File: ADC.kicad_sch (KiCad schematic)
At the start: 5 parts, among them J10 TBP03R2-350-03BE, J7 TBP03R2-350-03BE, J8 TBP03R2-350-03BE, J9 TBP03R2-350-03BE, U4 ADS1115IDGS

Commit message: Worked on PCB Layout
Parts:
- J10, J7, J8, J9: footprint TBP03R2-350-03BE:CUI_TBP03R2-350-03BE -> TBP03R2_350_03BE(1):CUI_TBP03R2-350-03BE
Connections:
- removed net Signal: J10.2, J7.2, J8.2, J9.2, U4.4 (AIN0), U4.5 (AIN1), U4.6 (AIN2), U4.7 (AIN3)
- new net Signal 1: J7.2, U4.4 (AIN0)
- new net Signal 2: J8.2, U4.5 (AIN1)
- new net Signal 3: J9.2, U4.6 (AIN2)
- new net Signal 4: J10.2, U4.7 (AIN3)
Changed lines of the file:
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@@
+	(wire
+		(pts
+			(xy 139.7 85.09) (xy 139.7 78.74)
+		)
+		(stroke
+			(width 0)
+			(type default)
+		)
+	)
 	(wire
 		(pts
@@
 	(wire
 		(pts
+			(xy 135.89 62.23) (xy 106.68 62.23)
+		)
+		(stroke
+			(width 0)
+			(type default)
+		)
+	)
+	(wire
+		(pts
 			(xy 106.68 71.12) (xy 116.84 71.12)
 		)
@@
 	(wire
 		(pts
-			(xy 106.68 73.66) (xy 129.54 73.66)
-		)
-		(stroke
-			(width 0)
-			(type default)
-		)
-	)
-	(wire
-		(pts
 			(xy 127 64.77) (xy 127 76.2)
 		)
@@
 	(wire
 		(pts
-			(xy 129.54 76.2) (xy 139.7 76.2)
-		)
-		(stroke
-			(width 0)
-			(type default)
-		)
-	)
-	(wire
-		(pts
-			(xy 134.62 73.66) (xy 139.7 73.66)
-		)
-		(stroke
-			(width 0)
-			(type default)
-		)
-	)
-	(wire
-		(pts
 			(xy 106.68 76.2) (xy 127 76.2)
 		)
@@
 	(wire
 		(pts
-			(xy 106.68 62.23) (xy 134.62 62.23)
+			(xy 139.7 73.66) (xy 135.89 73.66)
 		)
 		(stroke
@@
 	(wire
 		(pts
+			(xy 127 87.63) (xy 149.86 87.63)
+		)
+		(stroke
+			(width 0)
+			(type solid)
+			(color 1 0 0 1)
+		)
+	)
+	(wire
+		(pts
 			(xy 106.68 85.09) (xy 139.7 85.09)
 		)
@@
 	(wire
 		(pts
-			(xy 127 87.63) (xy 149.86 87.63)
-		)
-		(stroke
-			(width 0)
-			(type solid)
-			(color 1 0 0 1)
-		)
-	)
-	(wire
-		(pts
 			(xy 106.68 87.63) (xy 127 87.63)
 		)
@@
 	(wire
 		(pts
+			(xy 135.89 73.66) (xy 135.89 62.23)
+		)
+		(stroke
+			(width 0)
+			(type default)
+		)
+	)
+	(wire
+		(pts
 			(xy 149.86 91.44) (xy 154.94 91.44)
 		)
@@
 	(wire
 		(pts
-			(xy 129.54 73.66) (xy 129.54 76.2)
+			(xy 116.84 48.26) (xy 116.84 59.69)
+		)
+		(stroke
+			(width 0)
+			(type default)
+			(color 255 0 0 1)
+		)
+	)
+	(wire
+		(pts
+			(xy 149.86 83.82) (xy 149.86 87.63)
+		)
+		(stroke
+			(width 0)
+			(type solid)
+			(color 1 0 0 1)
+		)
+	)
+	(wire
+		(pts
+			(xy 133.35 73.66) (xy 133.35 76.2)
+		)
+		(stroke
+			(width 0)
+			(type default)
+		)
+	)
+	(wire
+		(pts
+			(xy 106.68 73.66) (xy 133.35 73.66)
+		)
+		(stroke
+			(width 0)
+			(type default)
+		)
+	)
+	(wire
+		(pts
+			(xy 133.35 76.2) (xy 139.7 76.2)
 		)
 		(stroke
@@
 	(wire
 		(pts
-			(xy 116.84 48.26) (xy 116.84 59.69)
+			(xy 149.86 48.26) (xy 149.86 60.96)
 		)
 		(stroke
@@
 	(wire
 		(pts
-			(xy 149.86 83.82) (xy 149.86 87.63)
-		)
-		(stroke
-			(width 0)
-			(type solid)
-			(color 1 0 0 1)
-		)
-	)
-	(wire
-		(pts
-			(xy 149.86 48.26) (xy 149.86 60.96)
+			(xy 106.68 59.69) (xy 116.84 59.69)
 		)
 		(stroke
@@
 	(wire
 		(pts
-			(xy 134.62 62.23) (xy 134.62 73.66)
-		)
-		(stroke
-			(width 0)
-			(type default)
-		)
-	)
-	(wire
-		(pts
-			(xy 106.68 59.69) (xy 116.84 59.69)
-		)
-		(stroke
-			(width 0)
-			(type default)
-			(color 255 0 0 1)
-		)
-	)
-	(wire
-		(pts
 			(xy 127 76.2) (xy 127 87.63)
 		)
@@
 			(type solid)
 			(color 1 0 0 1)
-		)
-	)
-	(wire
-		(pts
-			(xy 139.7 85.09) (xy 139.7 78.74)
-		)
-		(stroke
-			(width 0)
-			(type default)
 		)
 	)
@@
 		)
 	)
-	(label "Signal"
-		(at 109.22 50.8 0)
+	(label "Signal 4"
+		(at 107.95 85.09 0)
 		(fields_autoplaced yes)
 		(effects
@@
 		)
 	)
+	(label "Signal 2"
+		(at 107.95 62.23 0)
+		(fields_autoplaced yes)
+		(effects
+			(font
+				(size 1.27 1.27)
+			)
+			(justify left bottom)
+		)
+	)
 	(label "GND"
 		(at 109.22 76.2 0)
@@
 		)
 	)
-	(label "Signal"
-		(at 109.22 62.23 0)
+	(label "Signal 3"
+		(at 107.95 73.66 0)
 		(fields_autoplaced yes)
 		(effects
@@
 		)
 	)
-	(label "Signal"
-		(at 109.22 73.66 0)
+	(label "Signal 1"
+		(at 107.95 50.8 0)
 		(fields_autoplaced yes)
 		(effects
@@
 	(label "GND"
 		(at 109.22 64.77 0)
-		(fields_autoplaced yes)
-		(effects
-			(font
-				(size 1.27 1.27)
-			)
-			(justify left bottom)
-		)
-	)
-	(label "Signal"
-		(at 109.22 85.09 0)
 		(fields_autoplaced yes)
 		(effects
@@
 			)
 		)
-		(property "Footprint" "TBP03R2-350-03BE:CUI_TBP03R2-350-03BE"
+		(property "Footprint" "TBP03R2_350_03BE(1):CUI_TBP03R2-350-03BE"
 			(at 96.52 73.66 0)
 			(effects
@@
 			)
 		)
-		(property "Footprint" "TBP03R2-350-03BE:CUI_TBP03R2-350-03BE"
+		(property "Footprint" "TBP03R2_350_03BE(1):CUI_TBP03R2-350-03BE"
 			(at 96.52 50.8 0)
 			(effects
@@
 			)
 		)
-		(property "Footprint" "TBP03R2-350-03BE:CUI_TBP03R2-350-03BE"
+		(property "Footprint" "TBP03R2_350_03BE(1):CUI_TBP03R2-350-03BE"
 			(at 96.52 62.23 0)
 			(effects
@@
 			)
 		)
-		(property "Footprint" "TBP03R2-350-03BE:CUI_TBP03R2-350-03BE"
+		(property "Footprint" "TBP03R2_350_03BE(1):CUI_TBP03R2-350-03BE"
 			(at 96.52 85.09 0)
 			(effects

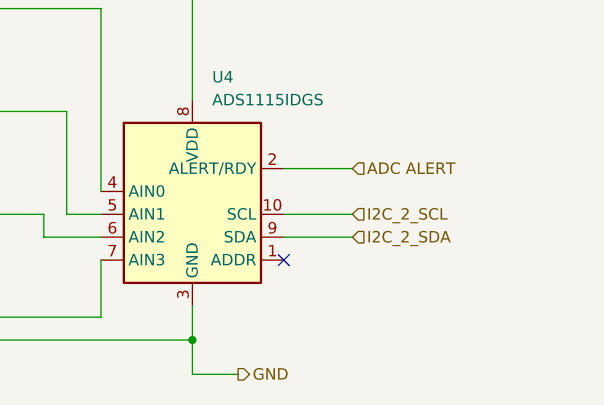
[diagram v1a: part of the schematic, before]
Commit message: Add debug pins and switch
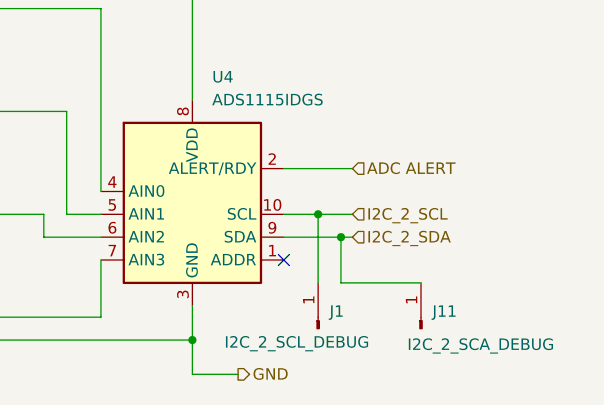
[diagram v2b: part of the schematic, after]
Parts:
- added J1: I2C_2_SCL_DEBUG, symbol Connector:Conn_01x01_Pin
- added J11: I2C_2_SCA_DEBUG, symbol Connector:Conn_01x01_Pin
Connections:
- net I2C_2_SCL: now also J1.1 (Pin_1)
- net I2C_2_SDA: now also J11.1 (Pin_1)
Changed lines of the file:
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@@
+	)
+	(junction
+		(at 166.37 76.2)
+		(diameter 0)
+		(color 0 0 0 0)
 	)
 	(junction
@@
 	)
 	(junction
+		(at 163.83 73.66)
+		(diameter 0)
+		(color 0 0 0 0)
+	)
+	(junction
 		(at 116.84 48.26)
 		(diameter 0)
@@
 	(wire
 		(pts
+			(xy 163.83 73.66) (xy 167.64 73.66)
+		)
+		(stroke
+			(width 0)
+			(type default)
+		)
+	)
+	(wire
+		(pts
 			(xy 116.84 48.26) (xy 149.86 48.26)
 		)
@@
 	(wire
 		(pts
-			(xy 160.02 73.66) (xy 167.64 73.66)
+			(xy 160.02 73.66) (xy 163.83 73.66)
 		)
 		(stroke
@@
 	(wire
 		(pts
+			(xy 106.68 50.8) (xy 139.7 50.8)
+		)
+		(stroke
+			(width 0)
+			(type default)
+		)
+	)
+	(wire
+		(pts
 			(xy 106.68 82.55) (xy 116.84 82.55)
 		)
@@
 			(type default)
 			(color 255 0 0 1)
+		)
+	)
+	(wire
+		(pts
+			(xy 166.37 81.28) (xy 175.26 81.28)
+		)
+		(stroke
+			(width 0)
+			(type default)
 		)
 	)
@@
 	(wire
 		(pts
-			(xy 106.68 50.8) (xy 139.7 50.8)
-		)
-		(stroke
-			(width 0)
-			(type default)
-		)
-	)
-	(wire
-		(pts
 			(xy 149.86 48.26) (xy 152.4 48.26)
 		)
@@
 	(wire
 		(pts
-			(xy 160.02 76.2) (xy 167.64 76.2)
+			(xy 160.02 76.2) (xy 166.37 76.2)
 		)
 		(stroke
@@
 	(wire
 		(pts
+			(xy 163.83 73.66) (xy 163.83 81.28)
+		)
+		(stroke
+			(width 0)
+			(type default)
+		)
+	)
+	(wire
+		(pts
 			(xy 135.89 73.66) (xy 135.89 62.23)
 		)
@@
 		(pts
 			(xy 106.68 73.66) (xy 133.35 73.66)
+		)
+		(stroke
+			(width 0)
+			(type default)
+		)
+	)
+	(wire
+		(pts
+			(xy 166.37 76.2) (xy 166.37 81.28)
+		)
+		(stroke
+			(width 0)
+			(type default)
+		)
+	)
+	(wire
+		(pts
+			(xy 166.37 76.2) (xy 167.64 76.2)
 		)
 		(stroke
@@
 					(unit 1)
 				)
+			)
+		)
+	)
+	(symbol
+		(lib_id "Connector:Conn_01x01_Pin")
+		(at 163.83 86.36 90)
+		(unit 1)
+		(exclude_from_sim no)
+		(in_bom yes)
+		(on_board yes)
+		(dnp no)
+		(property "Reference" "J1"
+			(at 165.1 84.4549 90)
+			(effects
+				(font
+					(size 1.27 1.27)
+				)
+				(justify right)
+			)
+		)
+		(property "Value" "I2C_2_SCL_DEBUG"
+			(at 153.416 87.884 90)
+			(effects
+				(font
+					(size 1.27 1.27)
+				)
+				(justify right)
+			)
+		)
+		(property "Footprint" ""
+			(at 163.83 86.36 0)
+			(effects
+				(font
+					(size 1.27 1.27)
+				)
+				(hide yes)
+			)
+		)
+		(property "Datasheet" "~"
+			(at 163.83 86.36 0)
+			(effects
+				(font
+					(size 1.27 1.27)
+				)
+				(hide yes)
+			)
+		)
+		(property "Description" "Generic connector, single row, 01x01, script generated"
+			(at 163.83 86.36 0)
+			(effects
+				(font
+					(size 1.27 1.27)
+				)
+				(hide yes)
+			)
+		)
+		(pin "1"
+		)
+		(instances
+			(project "Jetson_Extension_Board"
+				(path "/fac81d63-8655-47f4-bf8e-62708c29b8c6/607cc1b6-24e0-474a-81e8-dcba676951e3"
+					(reference "J1")
+					(unit 1)
+				)
+			)
+		)
+	)
+	(symbol
+		(lib_id "Connector:Conn_01x01_Pin")
+		(at 175.26 86.36 90)
+		(unit 1)
+		(exclude_from_sim no)
+		(in_bom yes)
+		(on_board yes)
+		(dnp no)
+		(property "Reference" "J11"
+			(at 176.53 84.4549 90)
+			(effects
+				(font
+					(size 1.27 1.27)
+				)
+				(justify right)
+			)
+		)
+		(property "Value" "I2C_2_SCA_DEBUG"
+			(at 173.736 88.138 90)
+			(effects
+				(font
+					(size 1.27 1.27)
+				)
+				(justify right)
+			)
+		)
+		(property "Footprint" ""
+			(at 175.26 86.36 0)
+			(effects
+				(font
+					(size 1.27 1.27)
+				)
+				(hide yes)
+			)
+		)
+		(property "Datasheet" "~"
+			(at 175.26 86.36 0)
+			(effects
+				(font
+					(size 1.27 1.27)
+				)
+				(hide yes)
+			)
+		)
+		(property "Description" "Generic connector, single row, 01x01, script generated"
+			(at 175.26 86.36 0)
+			(effects
+				(font
+					(size 1.27 1.27)
+				)
+				(hide yes)
+			)
+		)
+		(pin "1"
+		)
+		(instances
+			(project "Jetson_Extension_Board"
+				(path "/fac81d63-8655-47f4-bf8e-62708c29b8c6/607cc1b6-24e0-474a-81e8-dcba676951e3"
+					(reference "J11")
+					(unit 1)
+				)

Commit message: Revert "Add debug pins and switch"
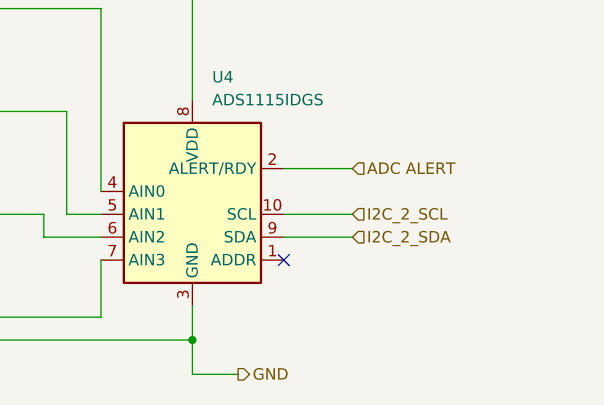
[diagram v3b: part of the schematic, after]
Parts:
- removed J1: I2C_2_SCL_DEBUG, symbol Connector:Conn_01x01_Pin
- removed J11: I2C_2_SCA_DEBUG, symbol Connector:Conn_01x01_Pin
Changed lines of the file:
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@@
-	)
-	(junction
-		(at 166.37 76.2)
-		(diameter 0)
-		(color 0 0 0 0)
 	)
 	(junction
@@
 	)
 	(junction
-		(at 163.83 73.66)
-		(diameter 0)
-		(color 0 0 0 0)
-	)
-	(junction
 		(at 116.84 48.26)
 		(diameter 0)
@@
 	(wire
 		(pts
-			(xy 163.83 73.66) (xy 167.64 73.66)
-		)
-		(stroke
-			(width 0)
-			(type default)
-		)
-	)
-	(wire
-		(pts
 			(xy 116.84 48.26) (xy 149.86 48.26)
 		)
@@
 	(wire
 		(pts
-			(xy 160.02 73.66) (xy 163.83 73.66)
+			(xy 160.02 73.66) (xy 167.64 73.66)
 		)
 		(stroke
@@
 	(wire
 		(pts
+			(xy 106.68 82.55) (xy 116.84 82.55)
+		)
+		(stroke
+			(width 0)
+			(type default)
+			(color 255 0 0 1)
+		)
+	)
+	(wire
+		(pts
+			(xy 116.84 71.12) (xy 116.84 82.55)
+		)
+		(stroke
+			(width 0)
+			(type default)
+			(color 255 0 0 1)
+		)
+	)
+	(wire
+		(pts
+			(xy 127 53.34) (xy 127 64.77)
+		)
+		(stroke
+			(width 0)
+			(type solid)
+			(color 1 0 0 1)
+		)
+	)
+	(wire
+		(pts
+			(xy 127 64.77) (xy 127 76.2)
+		)
+		(stroke
+			(width 0)
+			(type solid)
+			(color 1 0 0 1)
+		)
+	)
+	(wire
+		(pts
+			(xy 116.84 59.69) (xy 116.84 71.12)
+		)
+		(stroke
+			(width 0)
+			(type default)
+			(color 255 0 0 1)
+		)
+	)
+	(wire
+		(pts
 			(xy 106.68 50.8) (xy 139.7 50.8)
 		)
@@
 	(wire
 		(pts
-			(xy 106.68 82.55) (xy 116.84 82.55)
-		)
-		(stroke
-			(width 0)
-			(type default)
-			(color 255 0 0 1)
-		)
-	)
-	(wire
-		(pts
-			(xy 116.84 71.12) (xy 116.84 82.55)
-		)
-		(stroke
-			(width 0)
-			(type default)
-			(color 255 0 0 1)
-		)
-	)
-	(wire
-		(pts
-			(xy 166.37 81.28) (xy 175.26 81.28)
-		)
-		(stroke
-			(width 0)
-			(type default)
-		)
-	)
-	(wire
-		(pts
-			(xy 127 53.34) (xy 127 64.77)
-		)
-		(stroke
-			(width 0)
-			(type solid)
-			(color 1 0 0 1)
-		)
-	)
-	(wire
-		(pts
-			(xy 127 64.77) (xy 127 76.2)
-		)
-		(stroke
-			(width 0)
-			(type solid)
-			(color 1 0 0 1)
-		)
-	)
-	(wire
-		(pts
-			(xy 116.84 59.69) (xy 116.84 71.12)
-		)
-		(stroke
-			(width 0)
-			(type default)
-			(color 255 0 0 1)
-		)
-	)
-	(wire
-		(pts
 			(xy 149.86 48.26) (xy 152.4 48.26)
 		)
@@
 	(wire
 		(pts
-			(xy 160.02 76.2) (xy 166.37 76.2)
+			(xy 160.02 76.2) (xy 167.64 76.2)
 		)
 		(stroke
@@
 	(wire
 		(pts
-			(xy 163.83 73.66) (xy 163.83 81.28)
-		)
-		(stroke
-			(width 0)
-			(type default)
-		)
-	)
-	(wire
-		(pts
 			(xy 135.89 73.66) (xy 135.89 62.23)
 		)
@@
 		(pts
 			(xy 106.68 73.66) (xy 133.35 73.66)
-		)
-		(stroke
-			(width 0)
-			(type default)
-		)
-	)
-	(wire
-		(pts
-			(xy 166.37 76.2) (xy 166.37 81.28)
-		)
-		(stroke
-			(width 0)
-			(type default)
-		)
-	)
-	(wire
-		(pts
-			(xy 166.37 76.2) (xy 167.64 76.2)
 		)
 		(stroke
@@
 					(unit 1)
 				)
-			)
-		)
-	)
-	(symbol
-		(lib_id "Connector:Conn_01x01_Pin")
-		(at 163.83 86.36 90)
-		(unit 1)
-		(exclude_from_sim no)
-		(in_bom yes)
-		(on_board yes)
-		(dnp no)
-		(property "Reference" "J1"
-			(at 165.1 84.4549 90)
-			(effects
-				(font
-					(size 1.27 1.27)
-				)
-				(justify right)
-			)
-		)
-		(property "Value" "I2C_2_SCL_DEBUG"
-			(at 153.416 87.884 90)
-			(effects
-				(font
-					(size 1.27 1.27)
-				)
-				(justify right)
-			)
-		)
-		(property "Footprint" ""
-			(at 163.83 86.36 0)
-			(effects
-				(font
-					(size 1.27 1.27)
-				)
-				(hide yes)
-			)
-		)
-		(property "Datasheet" "~"
-			(at 163.83 86.36 0)
-			(effects
-				(font
-					(size 1.27 1.27)
-				)
-				(hide yes)
-			)
-		)
-		(property "Description" "Generic connector, single row, 01x01, script generated"
-			(at 163.83 86.36 0)
-			(effects
-				(font
-					(size 1.27 1.27)
-				)
-				(hide yes)
-			)
-		)
-		(pin "1"
-		)
-		(instances
-			(project "Jetson_Extension_Board"
-				(path "/fac81d63-8655-47f4-bf8e-62708c29b8c6/607cc1b6-24e0-474a-81e8-dcba676951e3"
-					(reference "J1")
-					(unit 1)
-				)
-			)
-		)
-	)
-	(symbol
-		(lib_id "Connector:Conn_01x01_Pin")
-		(at 175.26 86.36 90)
-		(unit 1)
-		(exclude_from_sim no)
-		(in_bom yes)
-		(on_board yes)
-		(dnp no)
-		(property "Reference" "J11"
-			(at 176.53 84.4549 90)
-			(effects
-				(font
-					(size 1.27 1.27)
-				)
-				(justify right)
-			)
-		)
-		(property "Value" "I2C_2_SCA_DEBUG"
-			(at 173.736 88.138 90)
-			(effects
-				(font
-					(size 1.27 1.27)
-				)
-				(justify right)
-			)
-		)
-		(property "Footprint" ""
-			(at 175.26 86.36 0)
-			(effects
-				(font
-					(size 1.27 1.27)
-				)
-				(hide yes)
-			)
-		)
-		(property "Datasheet" "~"
-			(at 175.26 86.36 0)
-			(effects
-				(font
-					(size 1.27 1.27)
-				)
-				(hide yes)
-			)
-		)
-		(property "Description" "Generic connector, single row, 01x01, script generated"
-			(at 175.26 86.36 0)
-			(effects
-				(font
-					(size 1.27 1.27)
-				)
-				(hide yes)
-			)
-		)
-		(pin "1"
-		)
-		(instances
-			(project "Jetson_Extension_Board"
-				(path "/fac81d63-8655-47f4-bf8e-62708c29b8c6/607cc1b6-24e0-474a-81e8-dcba676951e3"
-					(reference "J11")
-					(unit 1)
-				)

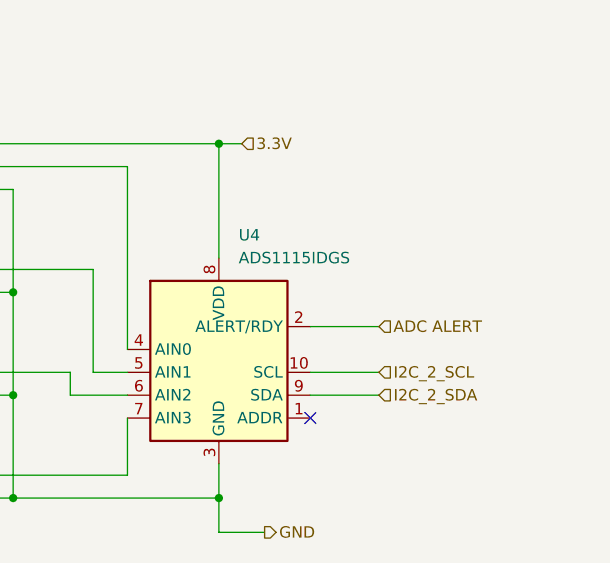
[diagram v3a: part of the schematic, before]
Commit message: debug pins schematic done and pcb partial
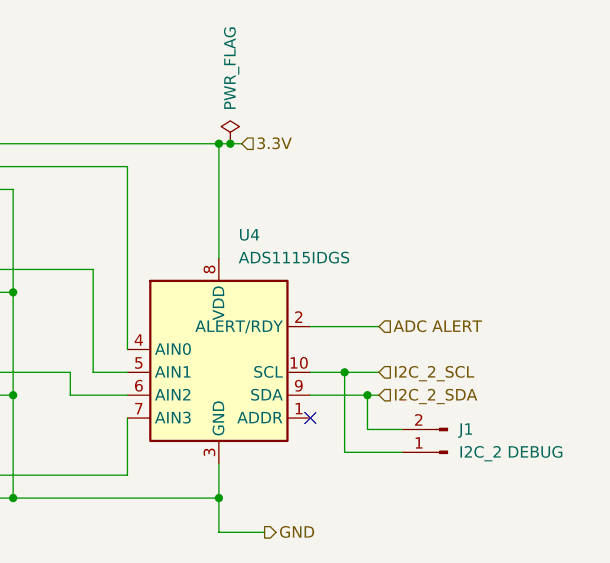
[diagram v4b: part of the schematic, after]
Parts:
- added J1: I2C_2 DEBUG, Connector_PinSocket_2.54mm:PinSocket_1x02_P2.54mm_Vertical, symbol Connector:Conn_01x02_Pin
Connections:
- net I2C_2_SCL: now also J1.1 (Pin_1)
- net I2C_2_SDA: now also J1.2 (Pin_2)
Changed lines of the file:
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@@
+	)
+	(junction
+		(at 151.13 48.26)
+		(diameter 0)
+		(color 0 0 0 0)
+	)
+	(junction
+		(at 166.37 76.2)
+		(diameter 0)
+		(color 0 0 0 0)
 	)
 	(junction
@@
 	)
 	(junction
+		(at 163.83 73.66)
+		(diameter 0)
+		(color 0 0 0 0)
+	)
+	(junction
 		(at 116.84 48.26)
 		(diameter 0)
@@
 	(wire
 		(pts
+			(xy 166.37 76.2) (xy 167.64 76.2)
+		)
+		(stroke
+			(width 0)
+			(type default)
+		)
+	)
+	(wire
+		(pts
+			(xy 163.83 73.66) (xy 167.64 73.66)
+		)
+		(stroke
+			(width 0)
+			(type default)
+		)
+	)
+	(wire
+		(pts
 			(xy 149.86 87.63) (xy 149.86 91.44)
 		)
@@
 	(wire
 		(pts
-			(xy 160.02 73.66) (xy 167.64 73.66)
+			(xy 160.02 73.66) (xy 163.83 73.66)
 		)
 		(stroke
@@
 	(wire
 		(pts
-			(xy 149.86 48.26) (xy 152.4 48.26)
+			(xy 149.86 48.26) (xy 151.13 48.26)
 		)
 		(stroke
@@
 	(wire
 		(pts
-			(xy 160.02 76.2) (xy 167.64 76.2)
+			(xy 166.37 80.01) (xy 170.18 80.01)
+		)
+		(stroke
+			(width 0)
+			(type default)
+		)
+	)
+	(wire
+		(pts
+			(xy 160.02 76.2) (xy 166.37 76.2)
 		)
 		(stroke
@@
 	(wire
 		(pts
+			(xy 163.83 82.55) (xy 170.18 82.55)
+		)
+		(stroke
+			(width 0)
+			(type default)
+		)
+	)
+	(wire
+		(pts
 			(xy 127 87.63) (xy 149.86 87.63)
 		)
@@
 	(wire
 		(pts
+			(xy 151.13 48.26) (xy 152.4 48.26)
+		)
+		(stroke
+			(width 0)
+			(type default)
+			(color 255 0 0 1)
+		)
+	)
+	(wire
+		(pts
 			(xy 135.89 73.66) (xy 135.89 62.23)
 		)
@@
 	(wire
 		(pts
+			(xy 163.83 73.66) (xy 163.83 82.55)
+		)
+		(stroke
+			(width 0)
+			(type default)
+		)
+	)
+	(wire
+		(pts
 			(xy 106.68 73.66) (xy 133.35 73.66)
 		)
@@
 			(type default)
 			(color 255 0 0 1)
+		)
+	)
+	(wire
+		(pts
+			(xy 166.37 76.2) (xy 166.37 80.01)
+		)
+		(stroke
+			(width 0)
+			(type default)
 		)
 	)
@@
 	)
 	(symbol
+		(lib_id "power:PWR_FLAG")
+		(at 151.13 48.26 0)
+		(unit 1)
+		(exclude_from_sim no)
+		(in_bom yes)
+		(on_board yes)
+		(dnp no)
+		(property "Reference" "#FLG05"
+			(at 151.13 46.355 0)
+			(effects
+				(font
+					(size 1.27 1.27)
+				)
+				(hide yes)
+			)
+		)
+		(property "Value" "PWR_FLAG"
+			(at 151.13 39.878 90)
+			(effects
+				(font
+					(size 1.27 1.27)
+				)
+			)
+		)
+		(property "Footprint" ""
+			(at 151.13 48.26 0)
+			(effects
+				(font
+					(size 1.27 1.27)
+				)
+				(hide yes)
+			)
+		)
+		(property "Datasheet" "~"
+			(at 151.13 48.26 0)
+			(effects
+				(font
+					(size 1.27 1.27)
+				)
+				(hide yes)
+			)
+		)
+		(property "Description" "Special symbol for telling ERC where power comes from"
+			(at 151.13 48.26 0)
+			(effects
+				(font
+					(size 1.27 1.27)
+				)
+				(hide yes)
+			)
+		)
+		(pin "1"
+		)
+		(instances
+			(project "Jetson_Extension_Board"
+				(path "/fac81d63-8655-47f4-bf8e-62708c29b8c6/607cc1b6-24e0-474a-81e8-dcba676951e3"
+					(reference "#FLG05")
+					(unit 1)
+				)
+			)
+		)
+	)
+	(symbol
 		(lib_id "Analog_ADC:ADS1115IDGS")
 		(at 149.86 73.66 0)
@@
 					(unit 1)
 				)
+			)
+		)
+	)
+	(symbol
+		(lib_id "Connector:Conn_01x02_Pin")
+		(at 175.26 82.55 180)
+		(unit 1)
+		(exclude_from_sim no)
+		(in_bom yes)
+		(on_board yes)
+		(dnp no)
+		(fields_autoplaced yes)
+		(property "Reference" "J1"
+			(at 176.53 80.0099 0)
+			(effects
+				(font
+					(size 1.27 1.27)
+				)
+				(justify right)
+			)
+		)
+		(property "Value" "I2C_2 DEBUG"
+			(at 176.53 82.5499 0)
+			(effects
+				(font
+					(size 1.27 1.27)
+				)
+				(justify right)
+			)
+		)
+		(property "Footprint" "Connector_PinSocket_2.54mm:PinSocket_1x02_P2.54mm_Vertical"
+			(at 175.26 82.55 0)
+			(effects
+				(font
+					(size 1.27 1.27)
+				)
+				(hide yes)
+			)
+		)
+		(property "Datasheet" "~"
+			(at 175.26 82.55 0)
+			(effects
+				(font
+					(size 1.27 1.27)
+				)
+				(hide yes)
+			)
+		)
+		(property "Description" "Generic connector, single row, 01x02, script generated"
+			(at 175.26 82.55 0)
+			(effects
+				(font
+					(size 1.27 1.27)
+				)
+				(hide yes)
+			)
+		)
+		(pin "1"
+		)
+		(pin "2"
+		)
+		(instances
+			(project ""
+				(path "/fac81d63-8655-47f4-bf8e-62708c29b8c6/607cc1b6-24e0-474a-81e8-dcba676951e3"
+					(reference "J1")
+					(unit 1)
+				)
